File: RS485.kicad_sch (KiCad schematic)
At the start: 9 parts, among them CN4 WJ15EDGRC-3.81-2P, U10 SIT3485ESA, U9 π131U30

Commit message: 更新六层电机控制板设计与器件库
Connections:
- net +5V_ISO is gone; now on net +3V3_ISO: C44.2, U9.16 (VDD2)
- net MCU_RS485_RXD: now also U9.3 (VIA); no longer U9.12 (VIC)
- net MCU_RS485_TX: now also U9.5 (VOC); no longer U9.3 (VIA)
- net RS485_RX: now also U9.12 (VIC); no longer U9.5 (VOC)
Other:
- moved on the sheet: CN4
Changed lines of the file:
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@@
 	(wire
 		(pts
+			(xy 144.145 62.23) (xy 133.35 62.23)
+		)
+		(stroke
+			(width 0)
+			(type default)
+		)
+	)
+	(wire
+		(pts
 			(xy 171.45 111.76) (xy 171.45 113.03)
 		)
@@
 	(wire
 		(pts
-			(xy 245.11 110.998) (xy 245.11 105.41)
+			(xy 243.84 111.125) (xy 243.84 105.41)
 		)
 		(stroke
@@
 	(wire
 		(pts
-			(xy 100.33 62.23) (xy 105.41 62.23)
-		)
-		(stroke
-			(width 0)
-			(type default)
-		)
-	)
-	(wire
-		(pts
 			(xy 171.45 91.44) (xy 171.45 95.25)
 		)
@@
 	(wire
 		(pts
+			(xy 92.075 62.23) (xy 105.41 62.23)
+		)
+		(stroke
+			(width 0)
+			(type default)
+		)
+	)
+	(wire
+		(pts
 			(xy 205.74 81.28) (xy 205.74 74.93)
 		)
@@
 	(wire
 		(pts
-			(xy 245.11 79.248) (xy 245.11 85.09)
+			(xy 243.84 78.74) (xy 243.84 85.09)
 		)
 		(stroke
@@
 	)
 	(label "RS485B"
-		(at 245.11 110.998 0)
-		(effects
-			(font
-				(size 1.27 1.27)
-			)
-			(justify left bottom)
-		)
-	)
-	(label "RS485_RX"
-		(at 133.35 62.23 0)
+		(at 243.84 111.125 0)
 		(effects
 			(font
@@
 	)
 	(label "RS485A"
-		(at 245.11 79.248 0)
+		(at 243.84 78.74 0)
 		(effects
 			(font
@@
 		)
 	)
-	(hierarchical_label "MCU_RS485_DE"
-		(shape input)
-		(at 87.63 46.99 90)
+	(label "RS485_RX"
+		(at 92.075 62.23 0)
+		(effects
+			(font
+				(size 1.27 1.27)
+			)
+			(justify left bottom)
+		)
+	)
+	(hierarchical_label "MCU_RS485_TX"
+		(shape output)
+		(at 144.145 62.23 90)
 		(effects
 			(font
@@
 		)
 	)
-	(hierarchical_label "MCU_RS485_RXD"
+	(hierarchical_label "MCU_RS485_DE"
 		(shape input)
-		(at 100.33 62.23 180)
+		(at 87.63 46.99 90)
 		(effects
 			(font
 				(size 1.27 1.27)
 			)
-			(justify right)
+			(justify left)
 		)
 	)
-	(hierarchical_label "MCU_RS485_TX"
+	(hierarchical_label "MCU_RS485_RXD"
 		(shape output)
 		(at 105.41 57.15 180)
@@
 	(symbol
 		(lib_id "WJ15EDGRC-3.81-2P:31330102")
-		(at 245.11 95.25 90)
+		(at 243.84 95.25 90)
 		(unit 1)
 		(body_style 1)
@@
 		(fields_autoplaced yes)
 		(property "Reference" "CN4"
-			(at 247.65 93.9799 90)
+			(at 246.38 93.9799 90)
 			(show_name no)
 			(do_not_autoplace no)
@@
 		)
 		(property "Value" "WJ15EDGRC-3.81-2P"
-			(at 247.65 96.5199 90)
+			(at 246.38 96.5199 90)
 			(show_name no)
 			(do_not_autoplace no)
@@
 		)
 		(property "Footprint" "kicad_api_lib:WJ15EDGRC-3.81-2P"
-			(at 241.3 95.25 0)
+			(at 240.03 95.25 0)
 			(hide yes)
 			(show_name no)
@@
 		)
 		(property "Datasheet" "http://file.elecfans.com/web1/M00/8F/66/o4YBAFzAJVGAapO-AAtZGykaSso280.pdf"
-			(at 241.3 95.25 0)
+			(at 240.03 95.25 0)
 			(hide yes)
 			(show_name no)
@@
 		)
 		(property "Description" "Plug and pull terminal board end/socket - closed 2Pin spacing: 3.81mm, 1 row of bent pins green"
-			(at 241.3 95.25 0)
+			(at 240.03 95.25 0)
 			(hide yes)
 			(show_name no)
@@
 		)
 		(property "MPN" "WJ15EDGRC-3.81-2P"
-			(at 245.11 95.25 0)
+			(at 243.84 95.25 0)
 			(hide yes)
 			(show_name no)
@@
 		)
 		(property "Manufacturer" "KANGNEX"
-			(at 245.11 95.25 0)
+			(at 243.84 95.25 0)
 			(hide yes)
 			(show_name no)
@@
 		)
 		(property "colour" "绿色"
-			(at 245.11 95.25 0)
+			(at 243.84 95.25 0)
 			(hide yes)
 			(show_name no)
@@
 		)
 		(property "connector_type" "板端/插座-闭口"
-			(at 245.11 95.25 0)
+			(at 243.84 95.25 0)
 			(hide yes)
 			(show_name no)
@@
 		)
 		(property "current" "7 A, 8 A"
-			(at 245.11 95.25 0)
+			(at 243.84 95.25 0)
 			(hide yes)
 			(show_name no)
@@
 		)
 		(property "flammability_rating" "UL94V-0"
-			(at 245.11 95.25 0)
+			(at 243.84 95.25 0)
 			(hide yes)
 			(show_name no)
@@
 		)
 		(property "holes_direction" "90°，直角"
-			(at 245.11 95.25 0)
+			(at 243.84 95.25 0)
 			(hide yes)
 			(show_name no)
@@
 		)
 		(property "huaqiu_pn" "G4189957"
-			(at 245.11 95.25 0)
+			(at 243.84 95.25 0)
 			(hide yes)
 			(show_name no)
@@
 		)
 		(property "lead_free" "Yes"
-			(at 245.11 95.25 0)
+			(at 243.84 95.25 0)
 			(hide yes)
 			(show_name no)
@@
 		)
 		(property "mount" "弯针"
-			(at 245.11 95.25 0)
+			(at 243.84 95.25 0)
 			(hide yes)
 			(show_name no)
@@
 		)
 		(property "number_of_rows" "1"
-			(at 245.11 95.25 0)
+			(at 243.84 95.25 0)
 			(hide yes)
 			(show_name no)
@@
 		)
 		(property "package" "弯插,P=3.81mm"
-			(at 245.11 95.25 0)
+			(at 243.84 95.25 0)
 			(hide yes)
 			(show_name no)
@@
 		)
 		(property "packaging" "500pcs"
-			(at 245.11 95.25 0)
+			(at 243.84 95.25 0)
 			(hide yes)
 			(show_name no)
@@
 		)
 		(property "pin_number_in_each_row" "2"
-			(at 245.11 95.25 0)
+			(at 243.84 95.25 0)
 			(hide yes)
 			(show_name no)
@@
 		)
 		(property "pins" "2"
-			(at 245.11 95.25 0)
+			(at 243.84 95.25 0)
 			(hide yes)
 			(show_name no)
@@
 		)
 		(property "pitch" "3.81 mm"
-			(at 245.11 95.25 0)
+			(at 243.84 95.25 0)
 			(hide yes)
 			(show_name no)
@@
 		)
 		(property "terminal_pitch" "3.81 mm"
-			(at 245.11 95.25 0)
+			(at 243.84 95.25 0)
 			(hide yes)
 			(show_name no)
@@
 		)
 		(property "termination_type" "插拔式接线端子"
-			(at 245.11 95.25 0)
+			(at 243.84 95.25 0)
 			(hide yes)
 			(show_name no)
@@
 		)
 		(property "voltage" "250 V, 300 V"
-			(at 245.11 95.25 0)
+			(at 243.84 95.25 0)
 			(hide yes)
 			(show_name no)
@@
 		(in_pos_files yes)
 		(dnp no)
-		(fields_autoplaced yes)
 		(property "Reference" "#PWR062"
 			(at 148.59 68.58 0)
@@
 			)
 		)
-		(property "Value" "+5V_ISO"
-			(at 148.59 59.69 0)
+		(property "Value" "+3V3_ISO"
+			(at 153.035 64.135 0)
 			(show_name no)
 			(do_not_autoplace no)
@@
 		(members "03a8f350-16e7-4e54-bb91-b1271fd25f7a" "23dfa473-4469-4f38-9314-589935e126c4"
 			"26108246-1be3-418f-a1b5-7bad52adde01" "297966c9-6dc6-4762-9531-585c081aefe6"
-			"2b41001d-9cc9-4632-a7f6-8042c0941b51" "31ddb25e-b6ab-4ced-8fe1-ae8fd7e62b07"
+			"2d089235-6bdc-46f2-aa82-44266913d394" "31ddb25e-b6ab-4ced-8fe1-ae8fd7e62b07"
 			"39d72b1f-3389-4232-b2b7-e1027b86fc17" "443484ec-33f8-42ee-8fbe-9dcb6f0eab62"
 			"51d99099-4acd-4cfe-9e93-c93f0b295e31" "55e09955-f414-4e01-bfcd-fa6c38337f1d"
@@
 			"62dfcb28-a389-46d6-ba56-12e3dff38496" "6395606e-565f-416a-b7f2-155000fc9816"
 			"6b1a0329-4171-4786-ab80-74d0023dd190" "74e8b89f-2b7b-4e33-af30-98d2808c7b00"
-			"7c5fdb95-2271-450f-9337-2569b4fe3a41" "85949e1d-b856-4582-aba4-5c2c3af4942d"
-			"911a547e-cc1d-4754-95f0-e97177cc3de2" "91c43ad4-cd65-4974-b441-99beb5d14579"
-			"91f5d9a9-d8d1-4523-9239-8b167ad28e6b" "9d5c04d1-a0da-457a-ba9b-5bc4c24853bf"
+			"78d53a6a-3820-44c9-b819-cc88946b892c" "7c5fdb95-2271-450f-9337-2569b4fe3a41"
+			"85949e1d-b856-4582-aba4-5c2c3af4942d" "911a547e-cc1d-4754-95f0-e97177cc3de2"
+			"91c43ad4-cd65-4974-b441-99beb5d14579" "91f5d9a9-d8d1-4523-9239-8b167ad28e6b"
 			"9e0f76fc-b6ad-415d-96c8-e3aea2d579fc" "9e2a6550-1d09-4560-bf3a-ec5f651006ee"
 			"a2c2a655-3083-4d99-9996-2dea564f73bf" "a9ec83d8-c6ab-43e8-be1c-8cf4f626aac8"
@@
 			"d8c2b88a-e5a2-4701-a8e7-d50ea2202197" "d94ab396-6e04-47c4-8b06-94bd16d04516"
 			"daebe6e3-4e2d-444b-b451-8a02f5898537" "e22e755f-e53a-4c4c-ab14-083374453ef6"
-			"ebf69372-e787-4354-a53e-7b597cbd503f" "ed190d79-050e-4e15-9d3c-59789546445f"
-			"eea1b2e9-26ed-4bef-9e3e-f096e30246c9" "ef2ebefc-983b-4848-9a18-9d586aee4b7c"
-			"f08841d5-75c3-41d6-b8de-9fecd535c3ce" "f54a7dd2-8bd2-499d-b4d6-678f2f426bd6"
+			"e5e22d6c-9dd5-41c5-b1b3-580624809164" "ebf69372-e787-4354-a53e-7b597cbd503f"
+			"ed190d79-050e-4e15-9d3c-59789546445f" "eea1b2e9-26ed-4bef-9e3e-f096e30246c9"
+			"ef2ebefc-983b-4848-9a18-9d586aee4b7c" "f08841d5-75c3-41d6-b8de-9fecd535c3ce"
+			"f54a7dd2-8bd2-499d-b4d6-678f2f426bd6" "f8756039-70e7-47c2-959a-d7ea0e1fb70a"
 			"fdd4bf25-51b0-4703-9236-d98b0b2e5368" "fde634bd-a756-4e03-b0ca-3d5b3de6ddfc"
 		)

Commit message: 更新电源与USB供电设计、PCB及器件库
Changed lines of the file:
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@@
 	(wire
 		(pts
-			(xy 144.145 62.23) (xy 133.35 62.23)
+			(xy 143.51 61.595) (xy 133.35 62.23)
 		)
 		(stroke
@@
 	(hierarchical_label "MCU_RS485_TX"
 		(shape output)
-		(at 144.145 62.23 90)
+		(at 143.51 61.595 0)
 		(effects
 			(font

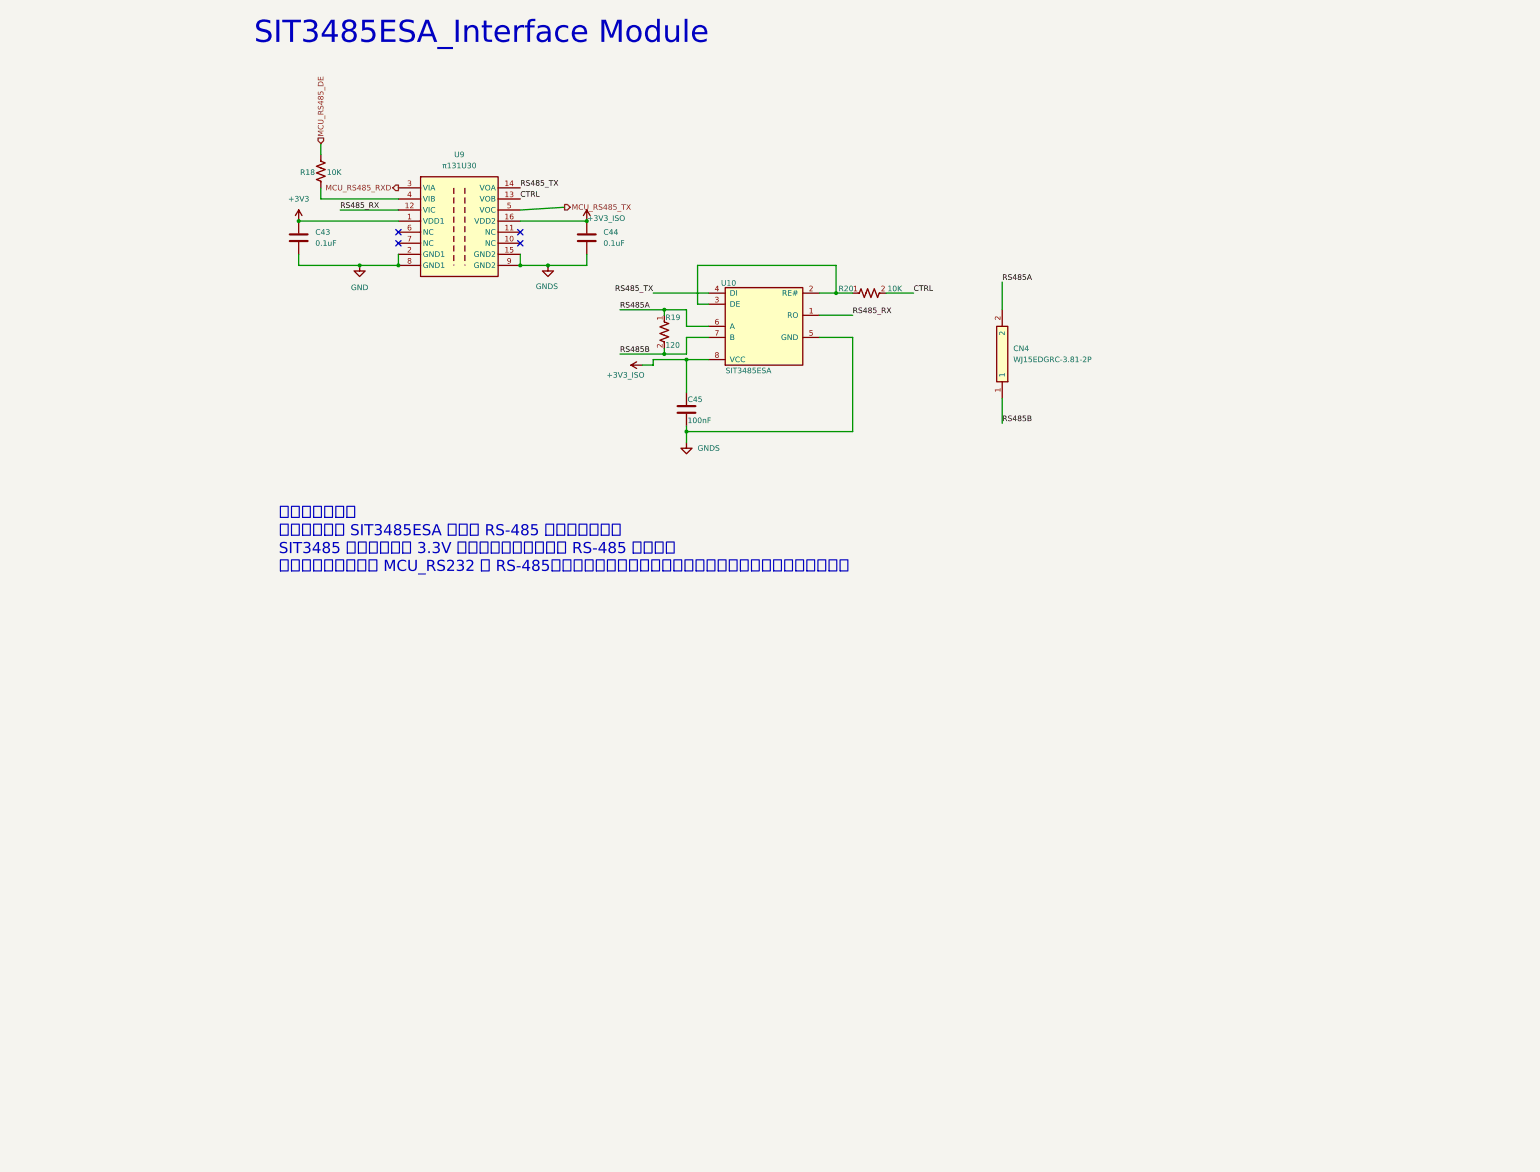
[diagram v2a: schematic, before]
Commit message: V2.0: sync KiCad design, add firmware snapshot and README
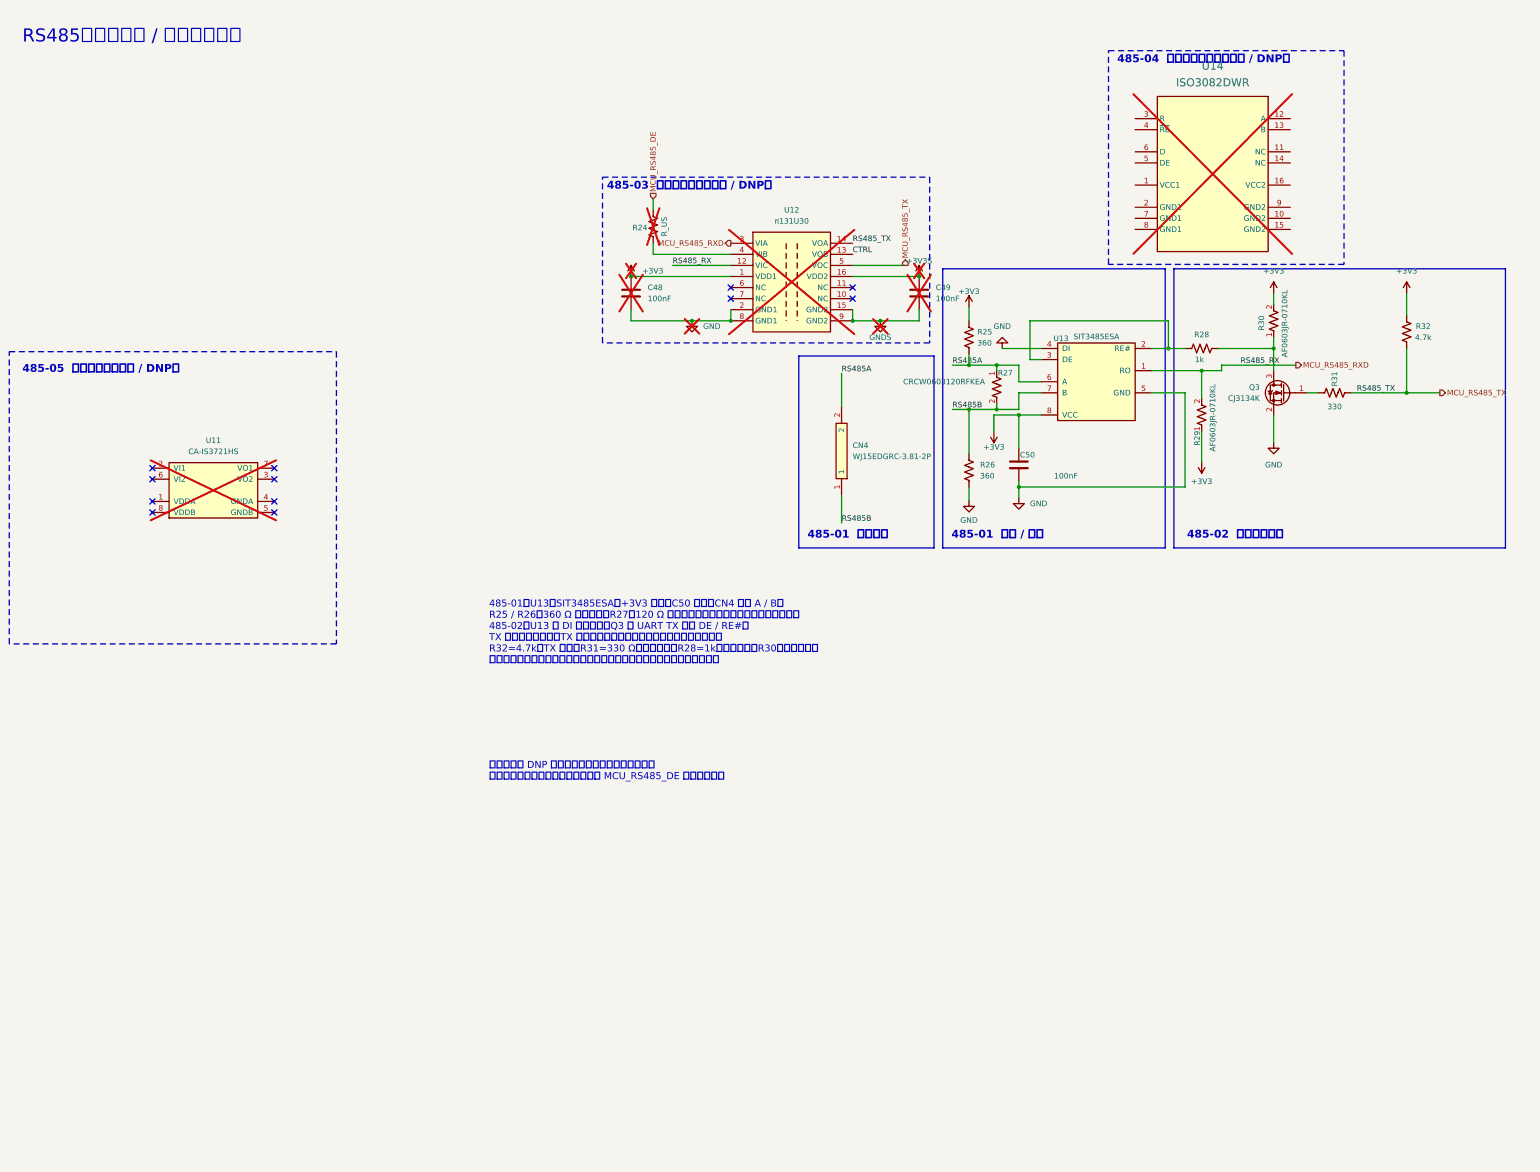
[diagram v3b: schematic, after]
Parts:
- added Q3: CJ3134K, kicad_api_lib:CJ3134K, symbol CJ3134K:MOS-N-1G2S3D-3
- added R25, R26: 360, Resistor_SMD:R_0603_1608Metric, symbol Device:R_US
- added R29, R30: AF0603JR-0710KL, Resistor_SMD:R_0603_1608Metric, symbol AF0603JR-0710KL:AF0603JR-0710KL
- added R31: 330, Resistor_SMD:R_0603_1608Metric, symbol Device:R_US
- added R32: 4.7k, Resistor_SMD:R_0603_1608Metric, symbol Device:R_US
- added U11: CA-IS3721HS, kicad_api_lib:CA-IS3721HS, symbol CA-IS3721HS:CA-IS3721HG
- added U14: ISO3082DWR, kicad_api_lib:ISO3082DWR, symbol ISO3082DWR:TI-ISO3082-SOIC_DW-16
- C48: renamed from C43; value 0.1uF -> 100nF; footprint Capacitor_SMD:C_0603_1608Metric_Pad1.08x0.95mm_HandSolder -> Capacitor_SMD:C_0603_1608Metric; now not fitted
- C49: renamed from C44; value 0.1uF -> 100nF; footprint Capacitor_SMD:C_0603_1608Metric_Pad1.08x0.95mm_HandSolder -> Capacitor_SMD:C_0603_1608Metric; now not fitted
- C50: renamed from C45; footprint Capacitor_SMD:C_0402_1005Metric_Pad0.74x0.62mm_HandSolder -> Capacitor_SMD:C_0603_1608Metric; symbol 0402X104K160CT:0402X104K160CT -> Project_Passives:CL10B104KB8NNNC_471bd30f; Capacitance (none) -> 100nF; Dielectric (none) -> X7R; MPN 0402X104K160CT -> CL10B104KB8NNNC; Manufacturer Walsin Technologies -> Samsung Electro-Mechanics; Tolerance (none) -> 10%; Voltage_Rating (none) -> 50V; body_length 1 mm -> (none); capacitance 100 nF -> (none); case_code_imperial 0402 -> (none); depth 500 µm -> (none); grade 消费级 -> (none); huaqiu_pn G4197523 -> (none); lead_free Lead Free -> (none); mount 表面贴装 -> (none); operating_temperature -55 °C, 85 °C -> (none); package 0402 -> 0603; packaging Tape and Reel -> (none); reach_svhc_compliant Unknown -> (none); temperature_characteristic X5R -> (none); terminal_pitch 0.75 mm -> (none); termination SMD -> (none); tolerance 10 % -> (none); voltage_rating 16 V -> (none)
- R24: renamed from R18; value 10K -> R_US; footprint Resistor_SMD:R_0603_1608Metric_Pad0.98x0.95mm_HandSolder -> Resistor_SMD:R_0603_1608Metric; now not fitted
- R27: renamed from R19; value 120 -> CRCW0603120RFKEA; footprint Resistor_SMD:R_0603_1608Metric_Pad0.98x0.95mm_HandSolder -> Resistor_SMD:R_0603_1608Metric
- R28: renamed from R20; value 10K -> 1k; footprint Resistor_SMD:R_0603_1608Metric_Pad0.98x0.95mm_HandSolder -> Resistor_SMD:R_0603_1608Metric; symbol AF0603JR-0710KL:AF0603JR-0710KL -> Device:R_US; MPN AF0603JR-0710KL -> (none); Manufacturer Yageo -> (none); Power (none) -> 0.1W; Tolerance (none) -> 1%; body_length 1.6 mm -> (none); body_width 0.8 mm -> (none); case_code_imperial 0603 -> (none); composition Thick Film -> (none); grade AEC-Q200 -> (none); height 0.022 in -> (none); height_overall 0.45 mm -> (none); huaqiu_pn G6606958 -> (none); lead_free Lead Free -> (none); mount SMT -> (none); number_of_terminations 2 -> (none); operating_temperature -55 °C -> (none); overload_voltage 75 V -> (none); package 0603 -> (none); packaging Tape and Reel -> (none); pins 2 -> (none); power_dissipation 100 mW -> (none); power_rating 100 mW -> (none); resistance 10 kΩ -> (none); temperature_coefficient 100 ppm/°C -> (none); tolerance 0.05 -> (none); type 厚膜电阻 -> (none)
- U12: renamed from U9; now not fitted
- U13: renamed from U10; footprint Package_SO:SOIC-8_3.9x4.9mm_P1.27mm -> kicad_api_lib:SIT3485ESA
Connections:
- net RS485_RX is gone; now on net MCU_RS485_RXD: U12.12 (VIC), U13.1 (RO)
- net +3V3: now also C50.1, U13.8 (VCC), R25.1, R29.1, R30.2, R32.1
- net CTRL: no longer R28.2
- net GND: now also C50.2, U13.4 (DI), U13.5 (GND), Q3.2 (S), R26.2
- net GNDS: no longer C50.2, U13.5 (GND)
- net MCU_RS485_RXD: now also R29.2
- net MCU_RS485_TX: now also U12.14 (VOA), R31.1, R32.2
- net RS485A: now also R25.2
- net RS485B: now also R26.1
- net +3V3_ISO renamed +3V3S
- net +3V3S: no longer C50.1, U13.8 (VCC)
- removed net RS485_TX: U12.14 (VOA), U13.4 (DI)
- new net: Q3.3 (D), R28.2, R30.1
- new net: Q3.1 (G), R31.2
- no-connect marks 4 -> 12
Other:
- note added: "485-01 偏置 / 收发"
- note added: "485-01 总线接口"
- note added: "485-01｜U13：SIT3485ESA，+3V3 供电；C50 去耦；CN4 引出 A / B。 R25 / R26：360 Ω 总线偏置；R27：120 Ω 端接，需结合总线位置与另一端端接配置。 485-02｜U13 的 DI 固定接地；Q3 由 UART TX 控制 DE / RE#。 TX 低：发送低电平；TX 高：释放总线并接收，高电平由总线偏置恢复。 R32=4.7k：TX 上拉；R31=330 Ω：栅极串阻；R28=1k：使能串阻；R30：使能上拉。 该方式的高电平边沿受偏置、端接与线缆电容影响，应按实际波特率验证。"
- note added: "485-02 自动方向控制"
- note added: "485-03 数字隔离预留【备用 / DNP】"
- note added: "485-04 隔离收发器预留【备用 / DNP】"
- note added: "485-05 隔离器备选【备用 / DNP】"
- note added: "RS485｜自动收发 / 备用隔离方案"
- note added: "虚线分区为 DNP 备用器件，不构成当前工作链路。 当前使用共地的自动收发方案；独立 MCU_RS485_DE 为预留信号。"
- note removed: "SIT3485ESA_Interface Module"
- note removed: "模块电路功能： 这是一个基于 SIT3485ESA 芯片的 RS-485 通信接口电路。 SIT3485 是一款常用的 3.3V 供电、半双工、低功耗 RS-485 收发器。 该电路的功能是实现 MCU_RS232 转 RS-485。它的设计标准且完整，包含了必要的去耦电容和终端电阻。"
- moved on the sheet: C50, CN4, R27, U13
